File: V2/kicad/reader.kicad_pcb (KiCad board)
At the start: 2 copper layers, 50 x 58.5 mm, 77 parts, among them U1 LM386M-1, U2 STM32F103C8T6, U3 MCP16301Hx-xCH, U4 TP3232N-SR, Y1 16MHz

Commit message: in process of making pcb
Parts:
- removed BOOT1: SW_SPDT, Button_Switch_SMD:SW_SPDT_PCM12
- removed C26: 100 nF, Capacitor_SMD:C_0402_1005Metric
- removed C27: 10 nF, Capacitor_SMD:C_0402_1005Metric
- removed JP1: SolderJumper_2_Bridged, Jumper:SolderJumper-2_P1.3mm_Bridged_RoundedPad1.0x1.5mm
- removed RC522: RFID RC522, UACS:PinSocket_1x08_P2.54mm_Vertical
- removed RJ12: 6P6C, Connector_RJ:RJ12_Amphenol_54601-x06_Horizontal
- removed TP1: +3.3 V, TestPoint:TestPoint_THTPad_D1.0mm_Drill0.5mm
- removed TP2: V+, TestPoint:TestPoint_THTPad_D1.0mm_Drill0.5mm
- removed TP3: Audio, TestPoint:TestPoint_THTPad_D1.0mm_Drill0.5mm
- removed TP4: GND, TestPoint:TestPoint_THTPad_D1.0mm_Drill0.5mm
- added BOOT2: SW_SPDT, Button_Switch_SMD:SW_SPDT_PCM12, F.Cu at (142.9, 64.9)
- added D7: PESD5V0U1BA,115, easyeda2kicad:SOD-323_L1.8-W1.3-LS2.5-BI, F.Cu at (160.3, 95.8)
- added D8: PMEG2010ER, Diode_SMD:Nexperia_CFP3_SOD-123W, F.Cu at (157.8, 92.9)
- added D9: B140-E3, Diode_SMD:D_SMA, F.Cu at (152.2, 77.2)
- added R18: 75 K, Resistor_SMD:R_0603_1608Metric, F.Cu at (154.2, 74.5)
- added R19: 5100 R, Resistor_SMD:R_0402_1005Metric, F.Cu at (153.7, 94.2)
- added R20: 5100 R, Resistor_SMD:R_0402_1005Metric, F.Cu at (155.9, 94.2)
- added R21: 24 K, Resistor_SMD:R_0603_1608Metric, F.Cu at (160.3, 82.6)
- added RC1: RFID RC522, UACS:PinSocket_1x08_P2.54mm_Vertical, F.Cu at (160.5, 30.5)
- added SW1: SW_Rezistance, easyeda2kicad:SW-SMD_SSSS812201, F.Cu at (178.2, 38.0)
- added SW2: SW_src, Button_Switch_SMD:SW_SPDT_PCM12, F.Cu at (178.1, 49.1)
- added TP6: +5V, TestPoint:TestPoint_THTPad_D1.0mm_Drill0.5mm, F.Cu at (235.6, 49.9)
- added TP7: +3.3 V, TestPoint:TestPoint_THTPad_D1.0mm_Drill0.5mm, F.Cu at (238.7, 50.9)
- added TP8: GND, TestPoint:TestPoint_THTPad_D1.0mm_Drill0.5mm, F.Cu at (238.4, 56.6)
- added TP9: RFID_IRQ, TestPoint:TestPoint_THTPad_D1.0mm_Drill0.5mm, F.Cu at (238.9, 53.8)
- added U5: ESD2CAN24-ES, easyeda2kicad:SOT-23-3_L2.9-W1.3-P1.90-LS2.4-BR, F.Cu at (173.0, 85.3)
- added U6: RJ-064-1, easyeda2kicad:CONN-SMD_RJ-064, F.Cu at (173.0, 94.9)
- added U7: MCP16301Hx-xCH, Package_TO_SOT_SMD:SOT-23-6, F.Cu at (153.6, 81.6)
- C10: value 10 nF -> 100 nF
- C11: value 1 µF -> 100 nF
- C13: value 1 µF -> 10 pF
- C14: value 100 nF -> GRM155C80J225KE95D; footprint Capacitor_SMD:C_0402_1005Metric -> easyeda2kicad:C0402
- C15: value 10 µF -> GRM155C80J225KE95D; footprint Capacitor_SMD:C_0603_1608Metric -> easyeda2kicad:C0402
- C16: value 100 nF -> CL10B104KC8NNNC; footprint Capacitor_SMD:C_0402_1005Metric -> easyeda2kicad:C0603
- C17: value 10 µF -> CL10B104KC8NNNC; footprint Capacitor_SMD:C_0603_1608Metric -> easyeda2kicad:C0603
- C18, C19: value 100 nF -> 1 µF
- C2: value 10 µF -> 10 pF; footprint Capacitor_SMD:C_0603_1608Metric -> Capacitor_SMD:C_0402_1005Metric
- C20: value 100 nF -> 10 nF
- C21, C24, C25: value 100 nF -> 10 µF; footprint Capacitor_SMD:C_0402_1005Metric -> Capacitor_SMD:C_0603_1608Metric
- C4: value 10 pF -> CL10B104KC8NNNC; footprint Capacitor_SMD:C_0402_1005Metric -> easyeda2kicad:C0603
- C5: value 100 nF -> 10µF; footprint Capacitor_SMD:C_0402_1005Metric -> Capacitor_SMD:C_0603_1608Metric
- C6: value 100 nF -> 10 pF
- C7: value 100 nF -> 4.7nF; footprint Capacitor_SMD:C_0402_1005Metric -> easyeda2kicad:C0603
- C9: value 100 µF -> 100 nF; footprint Capacitor_SMD:C_1206_3216Metric -> Capacitor_SMD:C_0402_1005Metric
- D2: value B140-E3 -> PESD5V0U1BA,115; footprint Diode_SMD:D_SMA -> easyeda2kicad:SOD-323_L1.8-W1.3-LS2.5-BI
- D3: value 1N4148WS -> PMEG2010ER; footprint Diode_SMD:D_SOD-323 -> Diode_SMD:Nexperia_CFP3_SOD-123W
- D6: value PMEG2010ER -> 1N4148WS; footprint Diode_SMD:Nexperia_CFP3_SOD-123W -> Diode_SMD:D_SOD-323
- R1: value 20 K -> RC1206JR-07100KL; footprint Resistor_SMD:R_0402_1005Metric -> easyeda2kicad:R1206
- R10: value 10 K -> 120; footprint Resistor_SMD:R_0603_1608Metric -> easyeda2kicad:R0805
- R11: value 1500 R -> 120; footprint Resistor_SMD:R_0402_1005Metric -> easyeda2kicad:R0805
- R12: value 5100 R -> 10 K; footprint Resistor_SMD:R_0402_1005Metric -> Resistor_SMD:R_0603_1608Metric
- R13: value 5100 R -> 1500 R
- R14: value 180 R -> 330 R
- R15: value 180 R -> 560 R
- R16: value 180 R -> 56 R
- R17: value 82 K -> 68 R; footprint Resistor_SMD:R_0603_1608Metric -> Resistor_SMD:R_0402_1005Metric
- R2: value 5 K -> 10 K; footprint UACS:Potentiometer_Bourns_3314J_Vertical -> Resistor_SMD:R_0603_1608Metric
- R3: value 10 R -> 10 K; footprint Resistor_SMD:R_0402_1005Metric -> Resistor_SMD:R_0603_1608Metric
- R4: value 330 R -> RC0805FR-07634KL; footprint Resistor_SMD:R_0402_1005Metric -> easyeda2kicad:R0805
- R5: value 560 R -> 10 K
- R6: value 56 R -> 10 K; footprint Resistor_SMD:R_0402_1005Metric -> Resistor_SMD:R_0603_1608Metric
- R7: value 68 R -> 10 K; footprint Resistor_SMD:R_0402_1005Metric -> Resistor_SMD:R_0603_1608Metric
- R8: value 75 K -> 120; footprint Resistor_SMD:R_0603_1608Metric -> easyeda2kicad:R0805
- R9: value 24 K -> 120; footprint Resistor_SMD:R_0603_1608Metric -> easyeda2kicad:R0805
- SP_Conn1: footprint Connector_Molex:Molex_PicoBlade_53047-0210_1x02_P1.25mm_Vertical -> easyeda2kicad:CONN-TH_0530470210
- TP5: value RFID_IRQ -> CANL
- U1: value LM386M-1 -> STM32H523CET6; footprint Package_SO:SOIC-8_3.9x4.9mm_P1.27mm -> STM32H523CET6:LQFP48_STM
- U2: value STM32F103C8T6 -> MAX98357AETE+T; footprint Package_QFP:LQFP-48_7x7mm_P0.5mm -> easyeda2kicad:TQFN-16_L3.0-W3.0-P0.50-BL-EP1.5
- U3: value MCP16301Hx-xCH -> MLD-TF PUSH-H18; footprint Package_TO_SOT_SMD:SOT-23-6 -> easyeda2kicad:SD-SMD_MLD-TF-PUSH-H18
- U4: value TP3232N-SR -> TCAN1057AVDRQ1; footprint Package_SO:SOIC-16_3.9x9.9mm_P1.27mm -> easyeda2kicad:SOIC-8_L4.9-W3.9-P1.27-LS6.0-BL
- moved H1 152.7 mm to (277.2, 108.5)
- moved H3 134.6 mm to (277.2, 113.3)
- moved H2 121.5 mm to (277.2, 110.9)
- moved TP5 86.8 mm to (234.8, 55.3)
- moved LED2 77.2 mm to (143.1, 98.1), turned to -90 degrees
- moved LED1 71.8 mm to (143.1, 95.0), turned to -90 degrees
- moved SP_Conn1 62.5 mm to (145.7, 90.6)
- moved R16 61.7 mm to (146.0, 98.7), turned to 180 degrees
- moved R17 59.6 mm to (146.0, 97.6), turned to 180 degrees
- moved R4 58.1 mm to (145.5, 83.1), turned to -90 degrees
- moved USB-C1 57.8 mm to (155.3, 101.3), turned to 0 degrees
- moved R14 57.4 mm to (146.0, 95.6), turned to 180 degrees
- moved R15 56.9 mm to (146.0, 94.5), turned to 180 degrees
- moved R13 53.3 mm to (154.8, 94.2), turned to 90 degrees
- moved SWD1 52.7 mm to (142.5, 101.1)
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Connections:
- C1 pad 1: /HSE_IN -> Net-(U1-PH1-OSC_OUT)
- C10 pad 1: +3.3VA -> +3.3V
- C11 pad 1: +3.3VA -> +3.3V
- C12 pad 1: V+ -> +3.3V
- C13 pad 1: +3.3V -> Net-(U4-CANL)
- C14 pad 1: Net-(D3-K) -> Net-(C14-Pad1)
- C14 pad 2: Net-(D2-K) -> GND
- C15 pad 1: +3.3V -> Net-(C15-Pad1)
- C16 pad 1: NRST -> GND
- C16 pad 2: GND -> +5V
- C18 pad 1: Net-(U4-C1+) -> +3.3V
- C18 pad 2: Net-(U4-C1-) -> GND
- C19 pad 1: +3.3V -> Net-(U1-VDDA)
- C2 pad 1: +3.3V -> Net-(U1-PH0-OSC_IN)
- C20 pad 1: Net-(U4-C2+) -> Net-(U1-VDDA)
- C20 pad 2: Net-(U4-C2-) -> GND
- C21 pad 1: Net-(U4-VS+) -> +3.3V
- C22 pad 1: Net-(U4-VS-) -> Net-(D6-K)
- C22 pad 2: GND -> Net-(D9-K)
- C23 pad 1: +3.3V -> +5V
- C24 pad 1: Net-(C24-Pad1) -> +3.3V
- C25 pad 1: Net-(C25-Pad1) -> +3.3V
- C3 pad 1: +3.3V -> /NRST
- C4 pad 1: /HSE_OUT -> +3.3V
- C5 pad 1: +3.3V -> GND
- C5 pad 2: GND -> +3.3V
- C6 pad 1: +3.3V -> GND
- C6 pad 2: GND -> Net-(U4-CANH)
- C7 pad 1: +3.3V -> Net-(C7-Pad1)
- C8 pad 1: Net-(C8-Pad1) -> +3.3V
- C8 pad 2: Net-(C8-Pad2) -> GND
- C9 pad 1: Net-(C8-Pad1) -> +3.3V
- C9 pad 2: Net-(SP_Conn1-Pin_1) -> GND
- D1 pad 1: V+ -> +5V
- D1 pad 2: +3.3V -> Net-(D1-A)
- D2 pad 1: Net-(D2-K) -> Net-(D1-A)
- D3 pad 1: Net-(D3-K) -> /BOOT0
- D3 pad 2: +3.3V -> Net-(D3-A)
- D4 pad 1: V+ -> Net-(D4-K)
- D4 pad 2: Net-(D4-A) -> /NRST
- D5 pad 1: V+ -> +5V
- D5 pad 2: Net-(D5-A) -> +3.3V
- D6 pad 1: BOOT0 -> Net-(D6-K)
- D6 pad 2: Net-(D6-A) -> +3.3V
- FB1 pad 1: +3.3VA -> Net-(U1-VDDA)
- L1 pad 1: Net-(D2-K) -> Net-(D9-K)
- R1 pad 2: Net-(R1-Pad2) -> Net-(SW2-B)
- R10 pad 1: GND -> Net-(U4-CANL)
- R10 pad 2: Net-(BOOT1-A) -> Net-(C7-Pad1)
- R11 pad 1: USB_D+ -> Net-(U4-CANL)
- R11 pad 2: +3.3V -> Net-(C7-Pad1)
- R12 pad 1: GND -> Net-(U4-S)
- R12 pad 2: Net-(USB-C1-CC1) -> GND
- R13 pad 1: GND -> /USB_D+
- R13 pad 2: Net-(USB-C1-CC2) -> +3.3V
- R14 pad 1: AUDIO_PWM -> /LED_G1
- R14 pad 2: Net-(C24-Pad1) -> Net-(LED1-A2)
- R15 pad 1: Net-(C24-Pad1) -> /LED_R1
- R15 pad 2: Net-(C25-Pad1) -> Net-(LED1-A1)
- R16 pad 1: Net-(C25-Pad1) -> /LED_G2
- R16 pad 2: Net-(C26-Pad1) -> Net-(LED2-A2)
- R17 pad 1: GND -> /LED_R2
- R17 pad 2: Net-(JP1-A) -> Net-(LED2-A1)
- R2 pad 1: Net-(R1-Pad2) -> +3.3V
- R2 pad 2: Net-(U1-+) -> Net-(U3-DAT1)
- R3 pad 1: Net-(C8-Pad2) -> +3.3V
- R3 pad 2: GND -> Net-(U3-DAT2)
- R4 pad 1: LED_G1 -> /~{SPEAKER_ON/OFF}
- R4 pad 2: Net-(LED1-A2) -> Net-(U2-~{SD_MODE})
- R5 pad 1: LED_R1 -> +3.3V
- R5 pad 2: Net-(LED1-A1) -> /NRST
- R6 pad 1: LED_G2 -> /BOOT0
- R6 pad 2: Net-(LED2-A2) -> GND
- R7 pad 1: LED_R2 -> GND
- R7 pad 2: Net-(LED2-A1) -> Net-(BOOT2-A)
- R8 pad 1: +3.3V -> Net-(C7-Pad1)
- R8 pad 2: Net-(U3-Vfb) -> Net-(U4-CANH)
- R9 pad 1: Net-(U3-Vfb) -> Net-(C7-Pad1)
- R9 pad 2: GND -> Net-(U4-CANH)
- RESET1 pad 1: NRST -> /NRST
- SP_Conn1 pad 1: Net-(SP_Conn1-Pin_1) -> Net-(U2-OUTN)
- SP_Conn1 pad 2: GND -> Net-(U2-OUTP)
- SWD1 pad 1: SWDIO -> /SWDIO
- SWD1 pad 3: SWCLK -> /SWCLK
- SWD1 pad 5: TRACESWO -> /TRACESWO
- SWD1 pad 9: NRST -> /NRST
- TP5 pad 1: RFID_IRQ -> Net-(U4-CANL)
- U1 pad 1: unconnected-(U1-GAIN-Pad1) -> +3.3V
- U1 pad 2: GND -> unconnected-(U1-PC13-Pad2)
- U1 pad 3: Net-(U1-+) -> unconnected-(U1-PC14-OSC32_IN-Pad3)
- U1 pad 4: GND -> unconnected-(U1-PC15-OSC32_OUT-Pad4)
- U1 pad 5: Net-(C8-Pad1) -> Net-(U1-PH0-OSC_IN)
- U1 pad 6: V+ -> Net-(U1-PH1-OSC_OUT)
- U1 pad 7: unconnected-(U1-BYPASS-Pad7) -> /NRST
- U1 pad 8: unconnected-(U1-GAIN-Pad8) -> GND
- U2 pad 1: +3.3V -> /I2S_SDO
- U2 pad 10: unconnected-(U2-PA0-Pad10) -> Net-(U2-OUTN)
- U2 pad 11: unconnected-(U2-PA1-Pad11) -> GND
- U2 pad 13: RFID_IRQ -> unconnected-(U2-N.C.-Pad13)
- U2 pad 14: RFID_SDA -> /I2S_WS
- U2 pad 15: RFID_SCK -> GND
- U2 pad 16: RFID_MISO -> /I2S_BCLK
- U2 pad 17: RFID_MOSI -> GND
- U2 pad 2: unconnected-(U2-PC13-Pad2) -> /GAIN_SLOT
- U2 pad 3: unconnected-(U2-PC14-Pad3) -> GND
- U2 pad 4: unconnected-(U2-PC15-Pad4) -> Net-(U2-~{SD_MODE})
- U2 pad 5: /HSE_IN -> unconnected-(U2-N.C.-Pad5)
- U2 pad 6: /HSE_OUT -> unconnected-(U2-N.C.-Pad6)
- U2 pad 7: NRST -> +3.3V
- U2 pad 8: GND -> +3.3V
- U2 pad 9: +3.3VA -> Net-(U2-OUTP)
- U3 pad 1: Net-(D3-K) -> Net-(U3-DAT2)
- U3 pad 2: GND -> /SD_SS
- U3 pad 3: Net-(U3-Vfb) -> /SPI_MOSI
- U3 pad 4: V+ -> +3.3V
- U3 pad 5: V+ -> /SPI_SCK
- U3 pad 6: Net-(D2-K) -> GND
- U4 pad 1: Net-(U4-C1+) -> /FDCAN_TX
- U4 pad 2: Net-(U4-VS+) -> GND
- U4 pad 3: Net-(U4-C1-) -> +5V
- U4 pad 4: Net-(U4-C2+) -> /FDCAN_RX
- U4 pad 5: Net-(U4-C2-) -> +3.3V
- U4 pad 6: Net-(U4-VS-) -> Net-(U4-CANL)
- U4 pad 7: unconnected-(U4-T2OUT-Pad7) -> Net-(U4-CANH)
- U4 pad 8: unconnected-(U4-R2IN-Pad8) -> Net-(U4-S)
- USB-C1 pad A4: Net-(D4-A) -> Net-(D8-A)
- USB-C1 pad A6: USB_D+ -> /USB_D+
- USB-C1 pad A7: USB_D- -> /USB_D-
- USB-C1 pad A8: (no net) -> unconnected-(USB-C1-SBU1-PadA8)
- USB-C1 pad A9: Net-(D4-A) -> Net-(D8-A)
- USB-C1 pad B4: Net-(D4-A) -> Net-(D8-A)
- USB-C1 pad B6: USB_D+ -> /USB_D+
- USB-C1 pad B7: USB_D- -> /USB_D-
- USB-C1 pad B8: (no net) -> unconnected-(USB-C1-SBU2-PadB8)
- USB-C1 pad B9: Net-(D4-A) -> Net-(D8-A)
- Y1 pad 1: /HSE_IN -> Net-(U1-PH1-OSC_OUT)
- Y1 pad 3: /HSE_OUT -> Net-(U1-PH0-OSC_IN)
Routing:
- net NRST: track 107.2 -> 0.00 mm, vias 4 -> 0
- net Net-(D6-A): track 81.5 -> 0.00 mm
- net +3.3V: track 151.2 -> 75.3 mm, vias 4 -> 0
- net V+: track 65.6 -> 0.00 mm, vias 3 -> 0
- net RFID_MOSI: track 52.8 -> 0.00 mm
- net LED_G2: track 50.9 -> 0.00 mm
- net LED_R2: track 50.1 -> 0.00 mm
- net USART3_RX: track 41.8 -> 0.00 mm
- net BOOT0: track 41.2 -> 0.00 mm
- net RFID_SDA: track 39.0 -> 0.00 mm
- net RFID_RST: track 38.8 -> 0.00 mm
- net RFID_SCK: track 37.5 -> 0.00 mm
- net RFID_MISO: track 34.2 -> 0.00 mm
- net TRACESWO: track 34.1 -> 0.00 mm, vias 2 -> 0
- net SWCLK: track 31.6 -> 0.00 mm, vias 2 -> 0
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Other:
- board size 50 x 58.5 mm -> 42 x 77 mm
- board text added: "2.0 2026/06"
- board text removed: "+"
- board text removed: "-"
- board text removed: "1"
- board text removed: "1.0 2025/04"
- board text removed: "2"
- board text removed: "3V3"
- board text removed: "Aud"
- board text removed: "B"
- board text removed: "BOOT"
- board text removed: "GND"
- board text removed: "GND X GND GND 3.3V"
- board text removed: "NRST X TRSW0 SWCLK SWDIO"
- board text removed: "P13"
- board text removed: "RESET"
- board text removed: "SWD"
- board text removed: "Speaker"
- board text removed: "Tested"
- board text removed: "V+"
- board text removed: "Vol"
- board text removed: "github.com/ostertag/UACS"

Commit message: pcb propably dones
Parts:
- added H4: MountingHole, MountingHole:ToolingHole_1.152mm, F.Cu at (169.6, 63.8)
- added TP1: DIN, UACS:TestPoint_Drill-1mm, F.Cu at (167.8, 52.5)
- added TP2: BCLK, UACS:TestPoint_Drill-1mm, F.Cu at (158.2, 62.7)
- added TP3: WS, UACS:TestPoint_Drill-1mm, F.Cu at (159.9, 57.0)
- added TP4: CANH, UACS:TestPoint_Drill-1mm, F.Cu at (138.8, 47.3)
- G***: moved to B.Cu
- TP5, TP6, TP7, TP8, TP9: footprint TestPoint:TestPoint_THTPad_D1.0mm_Drill0.5mm -> UACS:TestPoint_Drill-1mm
- moved H1 149.8 mm to (137.1, 55.3), turned to 180 degrees
- moved H2 134.4 mm to (162.7, 40.4), turned to 180 degrees
- moved H3 128.8 mm to (152.2, 82.1), turned to 180 degrees
- moved TP5 88.9 mm to (146.3, 47.3), turned to 180 degrees
- moved TP9 86.1 mm to (157.6, 82.2), turned to 180 degrees
- moved TP6 84.4 mm to (151.4, 44.3), turned to 180 degrees
- moved TP7 83.2 mm to (156.0, 60.7), turned to 180 degrees
- moved TP8 80.4 mm to (158.1, 58.9), turned to 180 degrees
- moved LED2 70.4 mm to (163.9, 30.9), turned to 180 degrees
- moved USB-C1 69.6 mm to (157.0, 31.8), turned to 180 degrees
- moved LED1 68.3 mm to (166.5, 30.9), turned to 180 degrees
- moved R16 67.2 mm to (163.4, 33.7), turned to 90 degrees
- moved R17 66.4 mm to (164.5, 33.7), turned to 90 degrees
- moved R14 65.0 mm to (166.0, 33.7), turned to 90 degrees
- moved R15 64.3 mm to (167.1, 33.7), turned to 90 degrees
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- renumbered BOOT2 to BOOT1, SP_Conn1 to SP_Con1
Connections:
- BOOT1 pad : (no net) -> GND
- SW1 pad SH: (no net) -> GND
- SW2 pad : (no net) -> GND
- U1 pad 11: /LED_R1 -> unconnected-(U1-PA1-Pad11)
- U1 pad 12: /LED_G1 -> unconnected-(U1-PA2-Pad12)
- U1 pad 38: /LED_R2 -> /LED_R1
- U1 pad 40: /LED_G2 -> /LED_G1
- U1 pad 41: unconnected-(U1-PB5-Pad41) -> /LED_R2
- U1 pad 42: unconnected-(U1-PB6-Pad42) -> /LED_G2
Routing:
- net +3.3V: track 75.3 -> 190.6 mm, vias 0 -> 2
- net /NRST: track 24.6 -> 80.6 mm, vias 1 -> 3
- net /LED_R1: track 0.00 -> 43.2 mm, vias 0 -> 2
- net /LED_G1: track 0.00 -> 43.0 mm, vias 0 -> 2
- net /LED_R2: track 0.00 -> 42.8 mm, vias 0 -> 2
- net /LED_G2: track 0.00 -> 41.9 mm, vias 0 -> 2
- net /BOOT0: track 0.00 -> 41.1 mm, vias 0 -> 4
- net /TRACESWO: track 0.00 -> 40.5 mm, vias 0 -> 3
- net /USB_D-: track 2.56 -> 42.1 mm, vias 0 -> 2
- net /GAIN_SLOT: track 0.00 -> 39.2 mm
- net /USB_D+: track 6.03 -> 44.2 mm, vias 0 -> 2
- net /I2S_WS: track 0.00 -> 34.9 mm, vias 0 -> 2
- net /SWCLK: track 0.00 -> 33.8 mm, vias 0 -> 3
- net GND: track 25.0 -> 57.7 mm, vias 3 -> 100
- net /I2S_SDO: track 0.00 -> 32.1 mm, vias 0 -> 2
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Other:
- board size 42 x 77 mm -> 42 x 61 mm

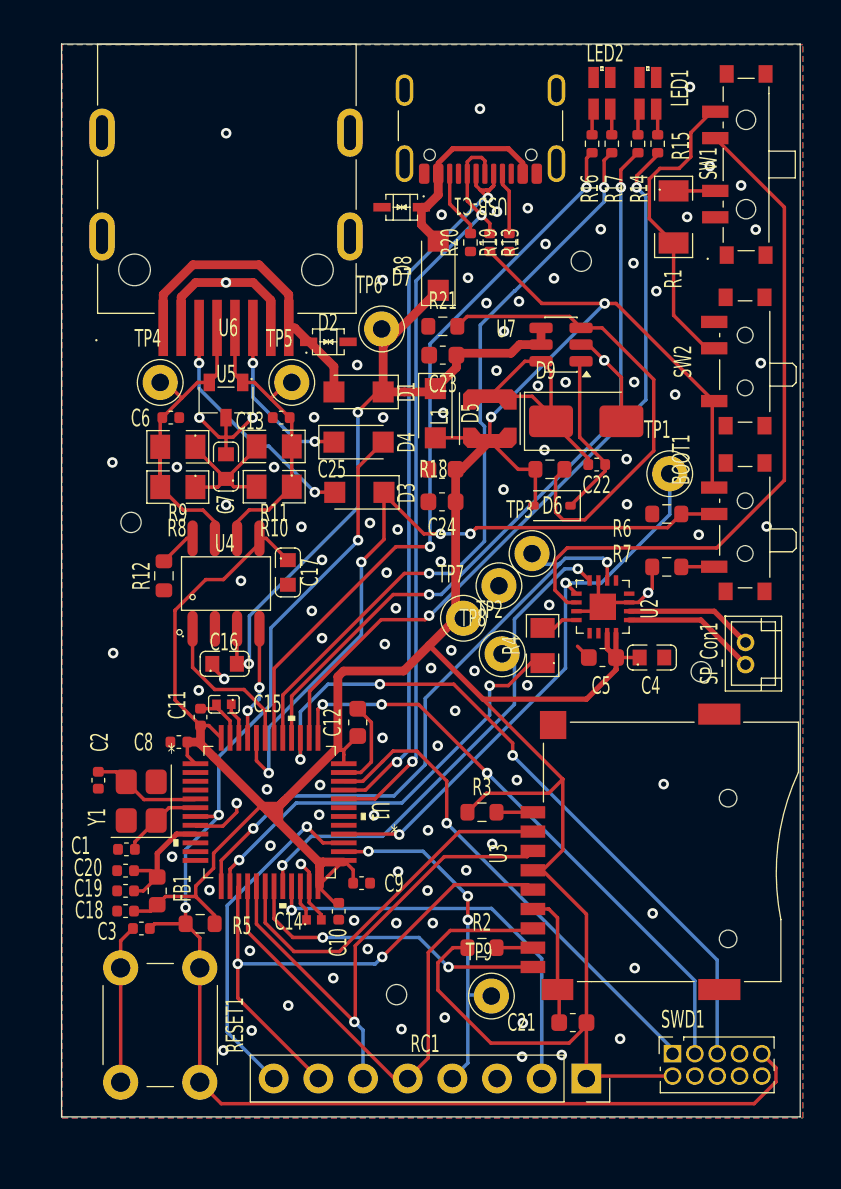
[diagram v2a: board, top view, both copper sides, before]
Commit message: changed debug connector to male, fixed 3d models not showing, moved sdcard slot invards by 2.3mm
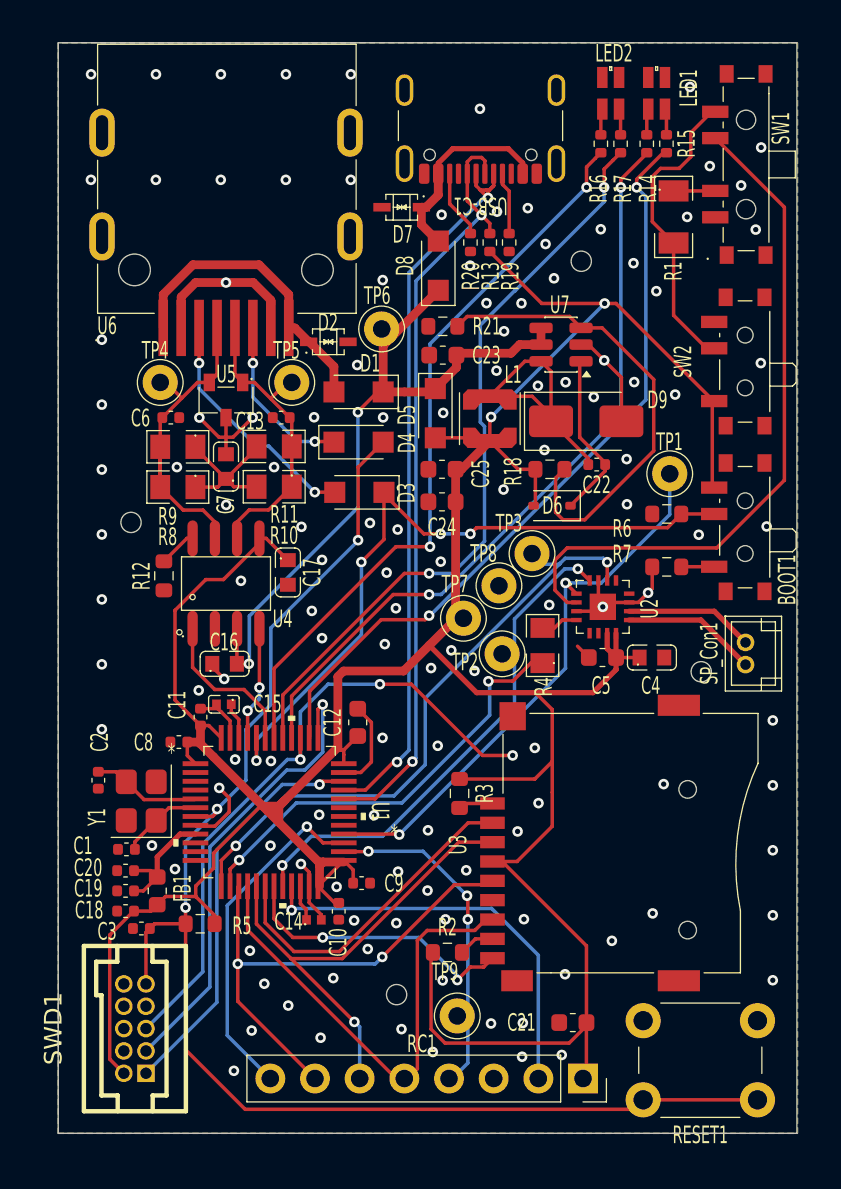
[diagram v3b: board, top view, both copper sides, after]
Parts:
- SWD1: value 2x5P, direct insert -> 1.27mm, male; footprint UACS:PinSocket_2x05_P1.27mm_Vertical -> easyeda2kicad:CONN-TH_IDC1.27-UP1S-5A
- moved SWD1 35.8 mm to (137.4, 84.0), turned to 90 degrees
- moved RESET1 32.6 mm to (172.8, 88.1), turned to 180 degrees
- moved U3 2.35 mm to (163.0, 73.5)
- moved TP9 2.25 mm to (155.7, 83.3)
- moved R2 1.98 mm to (155.1, 79.7)
- moved R3 1.66 mm to (155.8, 70.7), turned to -90 degrees
- moved LED1 0.50 mm to (167.0, 30.9)
- moved LED2 0.50 mm to (164.4, 30.9)
- moved R14 0.50 mm to (166.5, 33.7)
- moved R15 0.50 mm to (167.6, 33.7)
- moved R16 0.50 mm to (163.9, 33.7)
- moved R17 0.50 mm to (165.0, 33.7)
- moved RC1 0.19 mm to (154.0, 86.6)
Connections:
- BOOT1 pad : GND -> (no net)
- SW1 pad SH: GND -> (no net)
- SW2 pad : GND -> (no net)
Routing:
- net GND: track 57.7 -> 41.8 mm, vias 100 -> 127
- net /SWCLK: track 33.8 -> 26.5 mm, vias 3 -> 1
- net +3.3V: track 190.6 -> 197.6 mm
- net /SWDIO: track 27.8 -> 23.2 mm
- net /TRACESWO: track 40.5 -> 37.7 mm
- net /SPI_MOSI: track 30.1 -> 27.8 mm
- net /SPI_SCK: track 31.6 -> 29.4 mm
- net /SD_SS: track 20.8 -> 18.7 mm
- net /BOOT0: track 41.1 -> 39.7 mm
- net /SD_DETECTED: track 17.7 -> 16.4 mm
- net /RFID_IRQ: track 20.1 -> 18.9 mm
- net /SPI_MISO: track 29.2 -> 27.9 mm
- net /NRST: track 80.6 -> 80.0 mm
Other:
- board size 42 x 61 mm -> 42 x 62 mm

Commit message: .
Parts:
- turned R1 to 90 degrees
- renumbered SW2 to SWD1
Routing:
- net /TRACESWO: track 37.7 -> 20.6 mm, vias 3 -> 1
- net Net-(R1-Pad1): track 2.37 -> 4.18 mm
- net /SD_DETECTED: track 16.4 -> 17.3 mm
- net +3.3V: track 197.6 -> 196.8 mm
- net /SPI_MISO: track 27.9 -> 27.1 mm
- net /SPI_SCK: track 29.4 -> 28.6 mm
- net /SWDIO: track 23.2 -> 23.9 mm
- net Net-(SW2-B): track 16.7 -> 16.1 mm
- net /SD_SS: track 18.7 -> 19.3 mm
- net /LED_R1: track 43.6 -> 43.1 mm, vias 2 -> 3
- net GND: vias 127 -> 164
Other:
- board size 42 x 62 mm -> 42.5 x 62 mm
- board text added: "100K"
- board text added: "3V3"
- board text added: "Direct"
- board text added: "GND"
- board text added: "X"

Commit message: final touches
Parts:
- removed H4: MountingHole, MountingHole:ToolingHole_1.152mm
- removed SWD1: 1.27mm, male, easyeda2kicad:CONN-TH_IDC1.27-UP1S-5A
- added DEBUG: 1.27mm, male, easyeda2kicad:IDC-TH_10P-P1.27-X1270WV-2X05A-6TV01, F.Cu at (136.7, 82.8)
- added G***: LOGO, LOGO, B.Cu at (158.1, 73.8)
- BOOT1: value SW_SPDT -> BOOT
- RESET1: value SW_Push -> RESET
- TP3: value WS -> LRCLK
- TP7: value +3.3 V -> 3V3
- USB-C1: value USB_C_Receptacle_USB2.0_14P -> USB-C
- moved G*** 14.2 mm to (143.7, 64.8), turned to -90 degrees
- moved C3 4.38 mm to (139.9, 82.1), turned to -90 degrees
- moved C18 3.59 mm to (139.9, 79.2), turned to -90 degrees
- moved R5 1.91 mm to (142.5, 79.4), turned to -90 degrees
- moved FB1 1.62 mm to (140.2, 76.6)
- moved C19 1.48 mm to (138.2, 75.6)
- moved G*** 0.96 mm to (164.5, 40.3)
- moved H2 0.95 mm to (163.3, 41.2)
- moved C20 0.78 mm to (136.1, 75.0)
- moved LED1 0.60 mm to (167.0, 31.5)
- moved LED2 0.60 mm to (164.4, 31.5)
- moved R14 0.60 mm to (166.5, 34.3)
- moved R15 0.60 mm to (167.6, 34.3)
- moved R16 0.60 mm to (163.9, 34.3)
- moved R17 0.60 mm to (165.0, 34.3)
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- renumbered SWD1 to SW1, SP_Con1 to Speaker1
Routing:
- net /NRST: track 79.9 -> 96.3 mm
- net /SWDIO: track 23.9 -> 36.4 mm
- net /SWCLK: track 26.9 -> 38.4 mm
- net /TRACESWO: track 20.6 -> 31.3 mm
- net +3.3V: track 196.8 -> 189.8 mm
- net GND: track 41.8 -> 43.3 mm, vias 164 -> 183
- net /SPI_SCK: track 28.6 -> 29.5 mm
- net Net-(U1-VDDA): track 6.97 -> 7.71 mm
- net /LED_R2: track 43.0 -> 42.4 mm
- net /LED_G1: track 43.2 -> 42.6 mm
- net /LED_G2: track 42.1 -> 41.5 mm
- net /LED_R1: track 43.1 -> 42.6 mm, vias 3 -> 2
- net Net-(U2-OUTP): track 7.67 -> 7.13 mm
- net Net-(U2-OUTN): track 7.35 -> 6.82 mm
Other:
- board text added: "DIRECT"
- board text added: "https://github.com/ostertag/UACS"
- board text removed: "Direct"

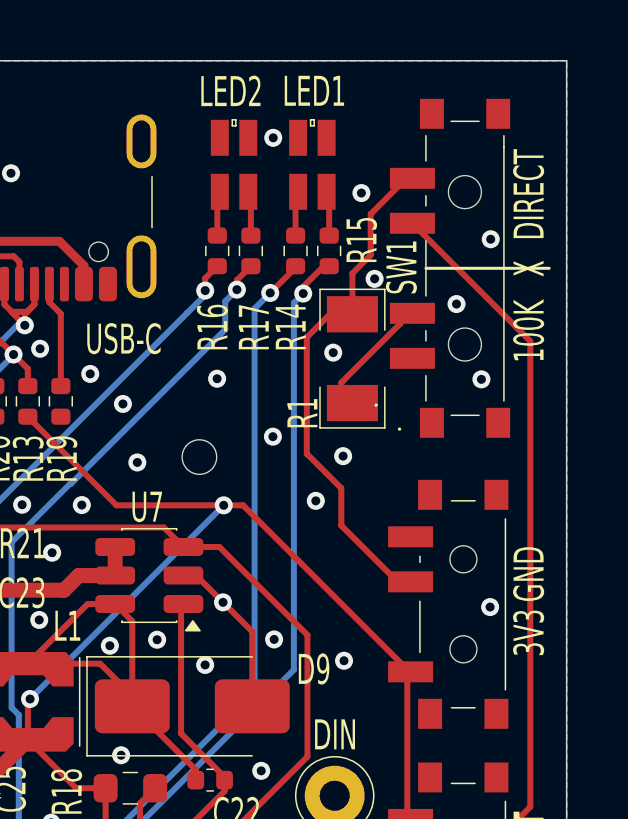
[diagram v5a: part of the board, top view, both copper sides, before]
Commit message: added switch combination table at the back, swapped 2 positions of SW1... X <-> 100K so it better fits pcb
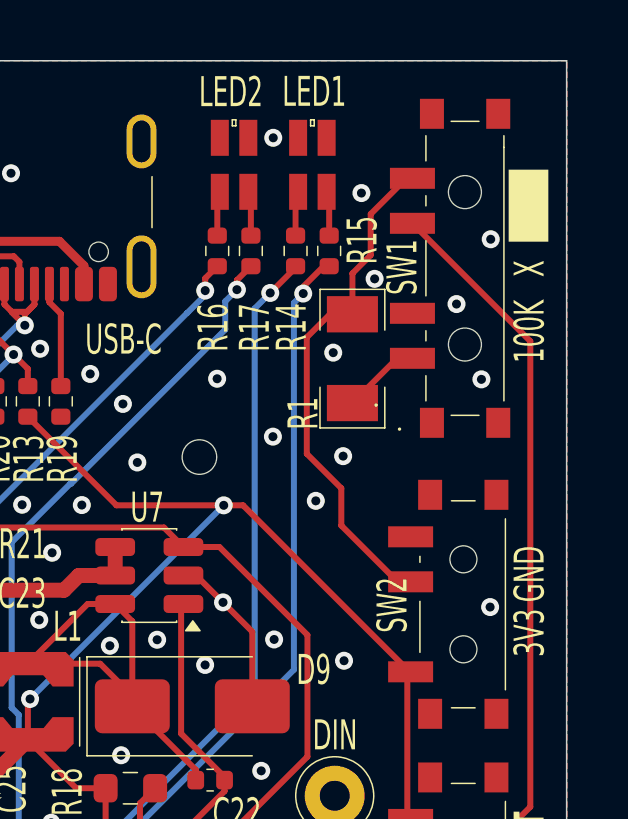
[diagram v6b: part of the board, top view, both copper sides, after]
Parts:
- moved G*** 31.0 mm to (138.1, 56.5), turned to 90 degrees
- moved G*** 4.12 mm to (162.1, 74.8)
- moved G*** 4.12 mm to (147.7, 65.8)
- renumbered SW1 to SW2
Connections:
- SW1 pad 1: unconnected-(SW1-Pad1) -> Net-(R1-Pad1)
- SW1 pad 2: Net-(R1-Pad1) -> (no net)
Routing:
- net Net-(R1-Pad1): track 3.78 -> 2.62 mm
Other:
- board text removed: "DIRECT"
